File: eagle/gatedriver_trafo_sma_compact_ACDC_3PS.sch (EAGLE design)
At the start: 25 parts, among them IC1 ISO1540, T1 TIP122V, T3 TIP122V, X1 BU-SMA-V

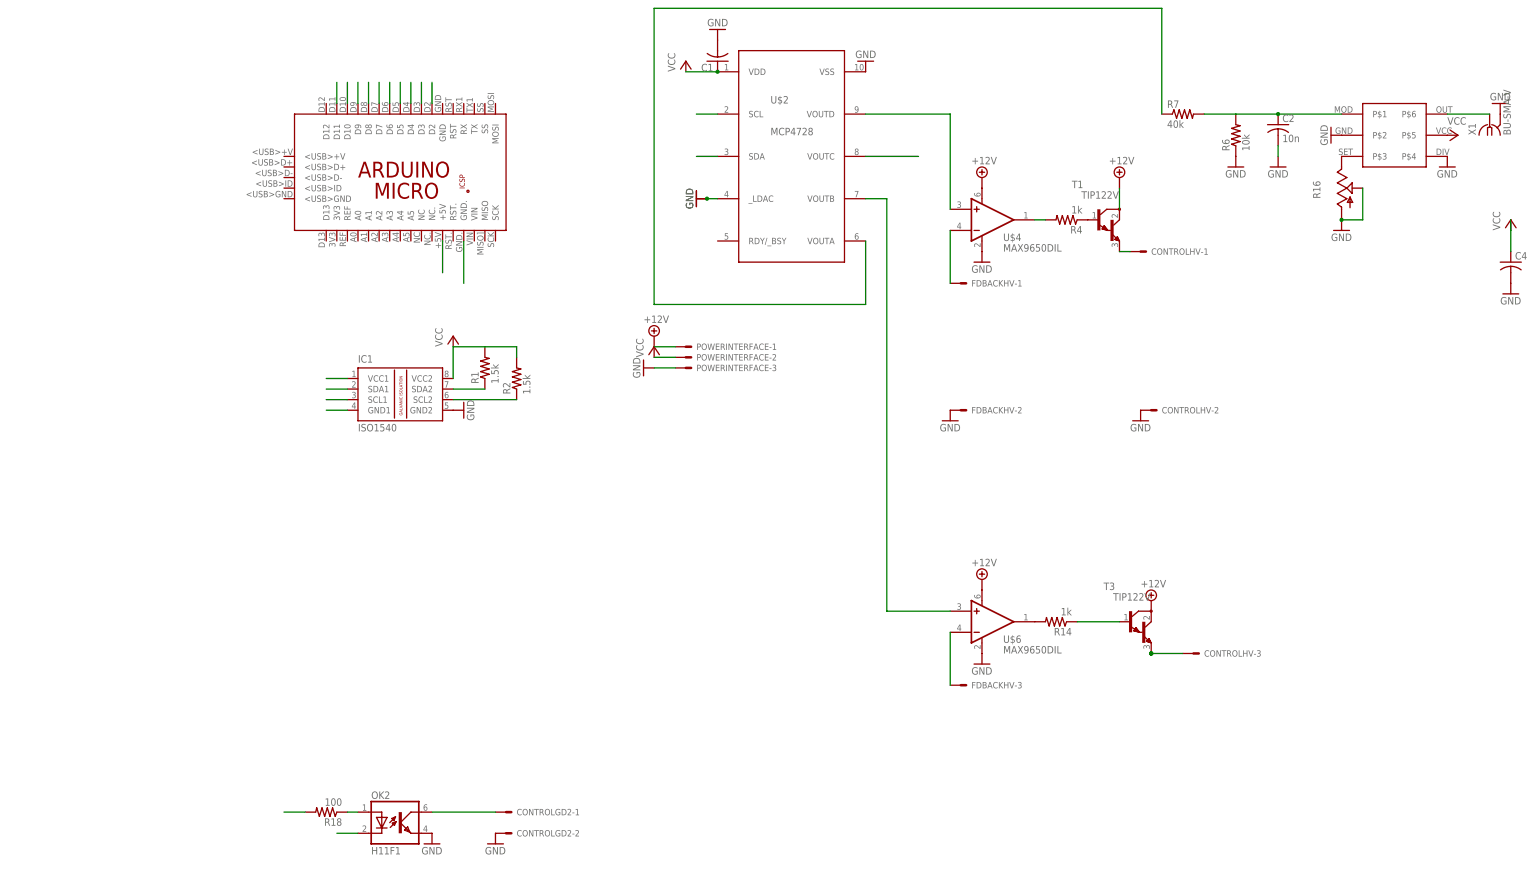
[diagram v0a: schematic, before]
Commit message: 3PS, 2 1kV in parallel
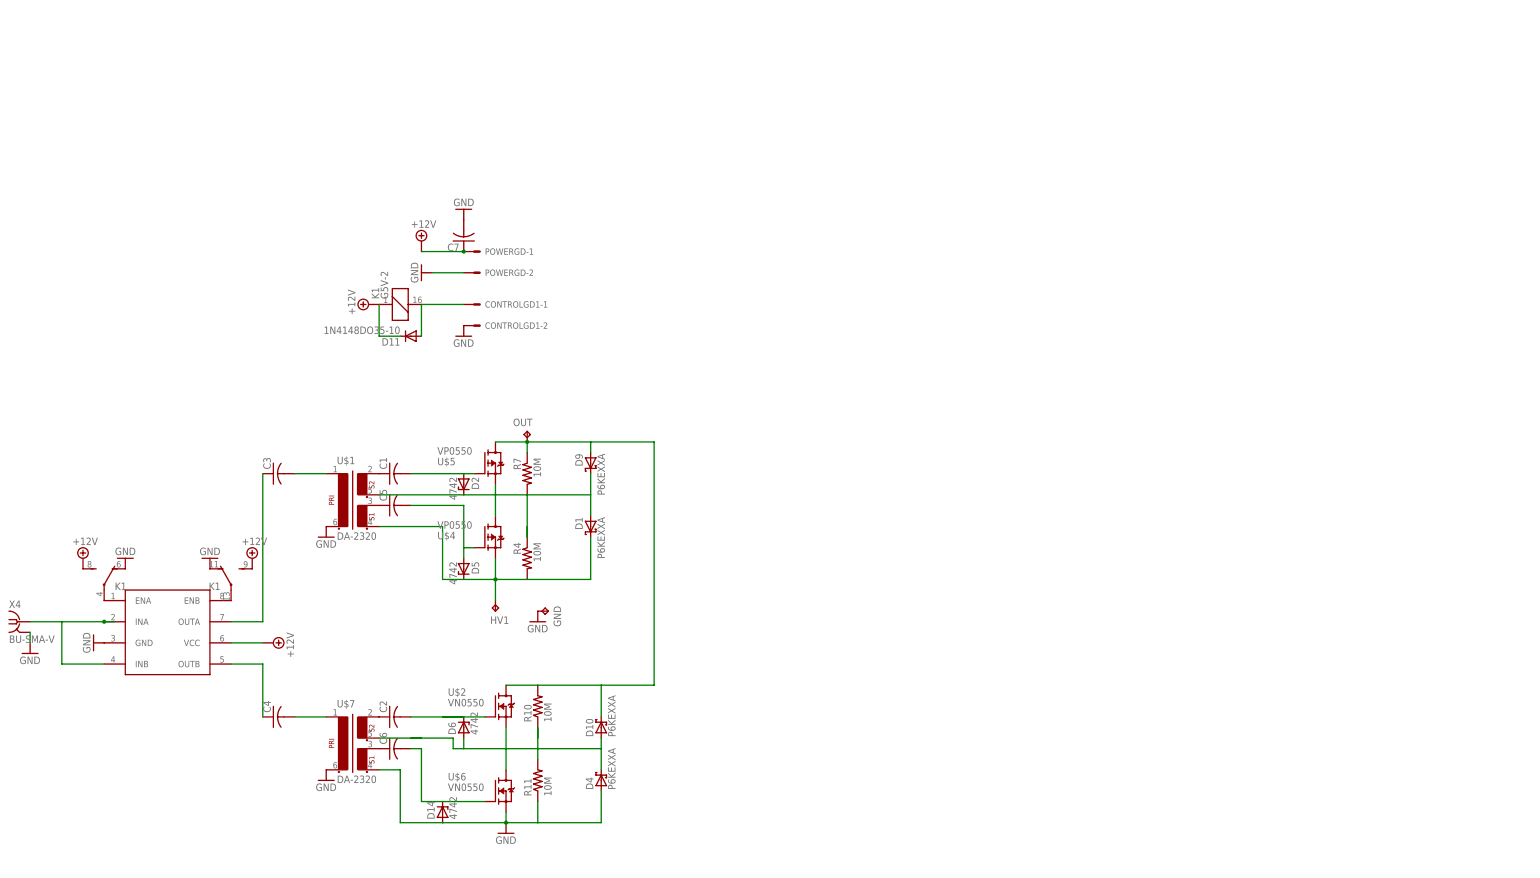
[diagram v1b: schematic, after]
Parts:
- removed CONTROLGD2: (no value), con-molex:KK-156-2
- removed CONTROLHV, FDBACKHV, POWERINTERFACE: (no value), con-molex:KK-156-3
- removed IC1: ISO1540, texas:ISO1540
- removed OK2: H11F1, optocoupler:H11F1
- removed PCB1: ARDUINO_MICRO, E14_Arduino_published:ARDUINO_MICRO
- removed R1, R2: 1.5k, resistor:R-US_0207/12
- removed R14: 1k, resistor:R-US_0207/12
- removed R16: (no value), pot:TRIM_US-B90P
- removed R18: 100, rcl:R-US_0207/12
- removed R6: 10k, resistor:R-US_0207/12
- removed T1, T3: TIP122V, transistor-npn:TIP122V
- removed X1: BU-SMA-V, con-coax:BU-SMA-V
- added C3, C5, C6: (no value), resistor:C-US050-055X075
- added C7: (no value), rcl:C-US050-030X075
- added CONTROLGD1, POWERGD: (no value), con-molex:KK-156-2
- added D1, D10, D4, D9: P6KEXXA, diode:P6KEXXA
- added D11: 1N4148DO35-10, diode:1N4148DO35-10
- added D14, D2, D5, D6: 4742, diode:ZENER-DIODEZD-10
- added GND, HV1, OUT: TPPAD1-20Y, testpad:TPPAD1-20Y
- added K1: G5V-2, relay:G5V-2
- added R10, R11: 10M, rcl:R-US_0207/12
- added U$3: UCC27425, texas:UCC27425
- added U$5: VP0550, transistor-fet:VP0550
- added U$7: DA-2320, trafo:DA-2320
- added X4: BU-SMA-V, con-coax:BU-SMA-V
- C1: device rcl:C-US050-050X075 -> resistor:C-US050-055X075
- C2: value 10n -> (none); device resistor:C-US050-024X044 -> resistor:C-US050-055X075
- C4: device resistor:C-US075-063X106 -> resistor:C-US050-055X075
- R4: value 1k -> 10M; device resistor:R-US_0207/12 -> rcl:R-US_0207/12
- R7: value 40k -> 10M; device resistor:R-US_0207/12 -> rcl:R-US_0207/12
- U$1: value LTC6992 -> DA-2320; device linear-technology:LTC6992 -> trafo:DA-2320
- U$2: value MCP4728DIL -> VN0550; device microchip:MCP4728DIL -> transistor-fet:VN0550
- U$4: value MAX9650DIL -> VP0550; device maxim:MAX9650DIL -> transistor-fet:VP0550
- U$6: value MAX9650DIL -> VN0550; device maxim:MAX9650DIL -> transistor-fet:VN0550
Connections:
- removed net +12V: POWERINTERFACE-1.S, T1.C, T3.C, U$4.V+, U$6.V+
- removed net A+5: IC1.VCC1, PCB1.+5V
- removed net AGND: IC1.GND1, PCB1.GND., R18.2
- removed net D10: PCB1.D10
- removed net D11: PCB1.D11
- removed net D4: PCB1.D4
- removed net D7: PCB1.D7
- removed net D8: PCB1.D8
- removed net ENSW2: CONTROLGD2-1.S, OK2.COL
- removed net N$12: R16.E, U$1.P$3
- removed net N$19: R4.2, U$4.OUT
- removed net N$8: FDBACKHV-1.S, U$4.-IN
- removed net PWM5: PCB1.D5
- removed net PWM6: PCB1.D6
- removed net PWM9: OK2.C, PCB1.D9
- removed net SCL: IC1.SCL1, PCB1.D3
- removed net SCL_OUT: IC1.SCL2, R2.1, U$2.SCL
- removed net SDA: IC1.SDA1, PCB1.D2
- removed net SDA_OUT: IC1.SDA2, R1.1, U$2.SDA
- removed net VCC: C1.1, C4.1, IC1.VCC2, POWERINTERFACE-2.S, R1.2, R2.2, U$1.P$5, U$2.VDD
- new net +15V: C7.1, D11.C, K11.S, K12.S, K1A.1, POWERGD-1.S, U$3.VCC
- new net ENSW: CONTROLGD1-1.S, D11.A, K1A.2
- new net N$11: C1.2, D2.A, U$5.G
- new net N$22: C2.1, U$7.6
- new net N$23: C6.1, U$7.4
- new net N$25: C2.2, D6.C, U$2.G
- new net N$27: C6.2, D14.C, U$6.G
- new net N$6: C4.2, U$7.1
- new net N$9: U$7.5
- net GND: now also C7.2, CONTROLGD1-2.S, D14.A, D4.A, GND.TP, K11.O, K12.O, POWERGD-2.S, R11.1, U$1.2, U$3.GND, U$6.S, U$7.2, U$7.3, X4.2; no longer C1.2, C2.2, C4.2, CONTROLGD2-2.S, CONTROLHV-2.S, FDBACKHV-2.S, IC1.GND2, OK2.EMIT, POWERINTERFACE-3.S, R16.A, R16.S, R6.1, U$1.P$2, U$1.P$4, U$2.VSS, U$2._LDAC, U$4.V-, U$6.V-, X1.2
- net N$1: now also U$3.INA, U$3.INB, X4.1; no longer R7.1, U$2.VOUTA
- net N$13: now also D10.A, D4.C, D6.A, R10.1, R11.2, U$2.S, U$6.D; no longer U$1.P$6, X1.1
- net N$14: now also K11.P, U$3.ENA; no longer FDBACKHV-3.S, U$6.-IN
- net N$15: now also K12.P, U$3.ENB; no longer R14.1, T3.B
- net N$16: now also C5.2, D5.A, U$4.G; no longer U$2.VOUTD, U$4.+IN
- net N$17: now also D1.C, D5.C, HV1.TP, R4.2, U$1.3, U$4.S; no longer U$2.VOUTC
- net N$18: now also D1.A, D2.C, D9.C, R4.1, R7.2, U$1.5, U$4.D, U$5.S; no longer U$2.VOUTB, U$6.+IN
- net N$2: now also C3.1, U$3.OUTA; no longer C2.1, R6.2, R7.2, U$1.P$1
- net N$21: now also D10.C, D9.A, OUT.TP, R10.2, R7.1, U$2.D, U$5.D; no longer R14.2, U$6.OUT
- net N$3: now also C3.2, U$1.1; no longer R4.1, T1.B
- net N$4: now also C4.1, U$3.OUTB; no longer CONTROLHV-1.S, T1.E
- net N$5: now also C1.1, U$1.6; no longer CONTROLHV-3.S, T3.E
- net N$7: now also C5.1, U$1.4; no longer OK2.A, R18.1
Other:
- moved on the sheet: C1, C2, C4, R4, R7

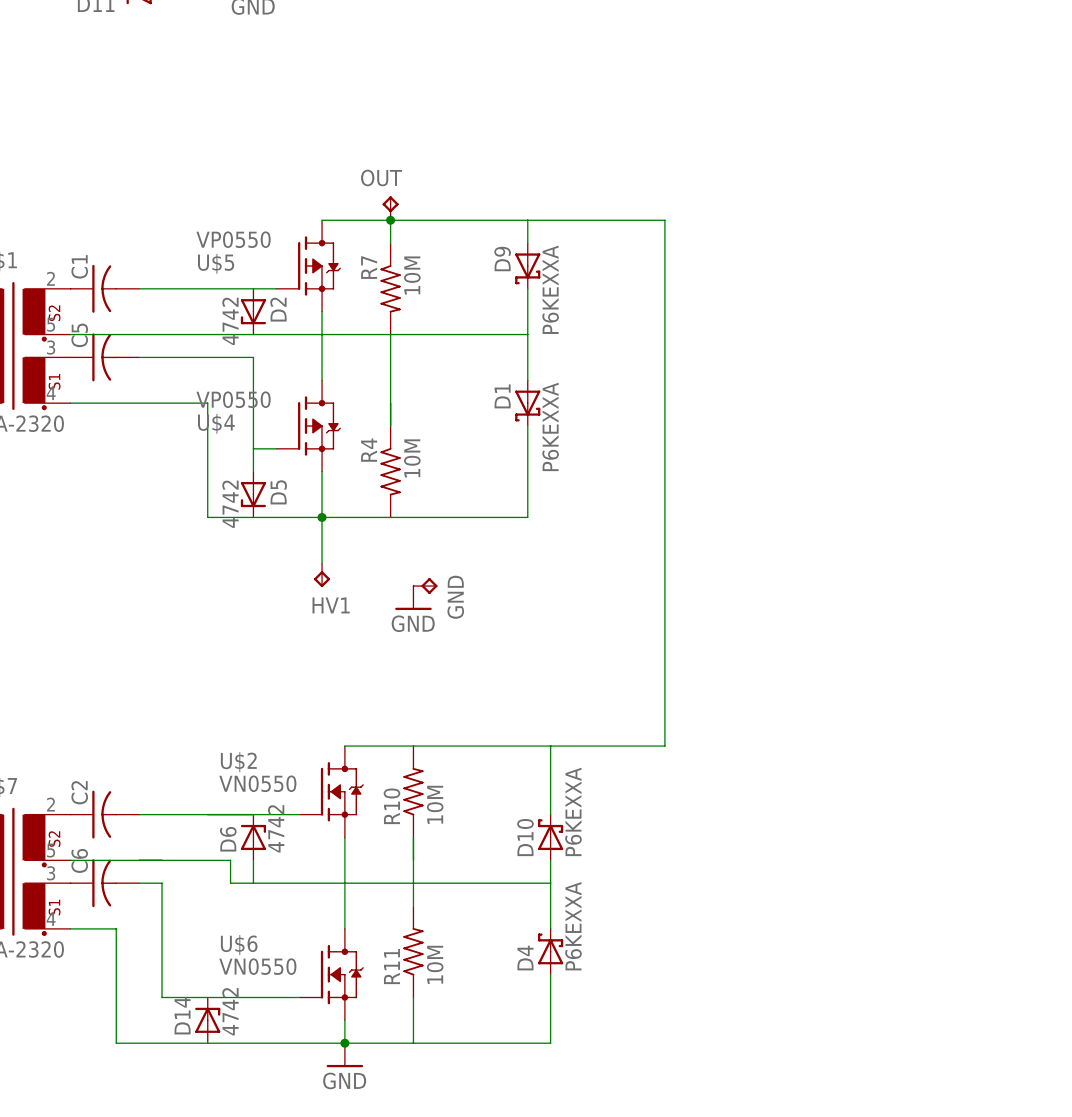
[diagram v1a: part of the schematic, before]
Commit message: capacitor bank
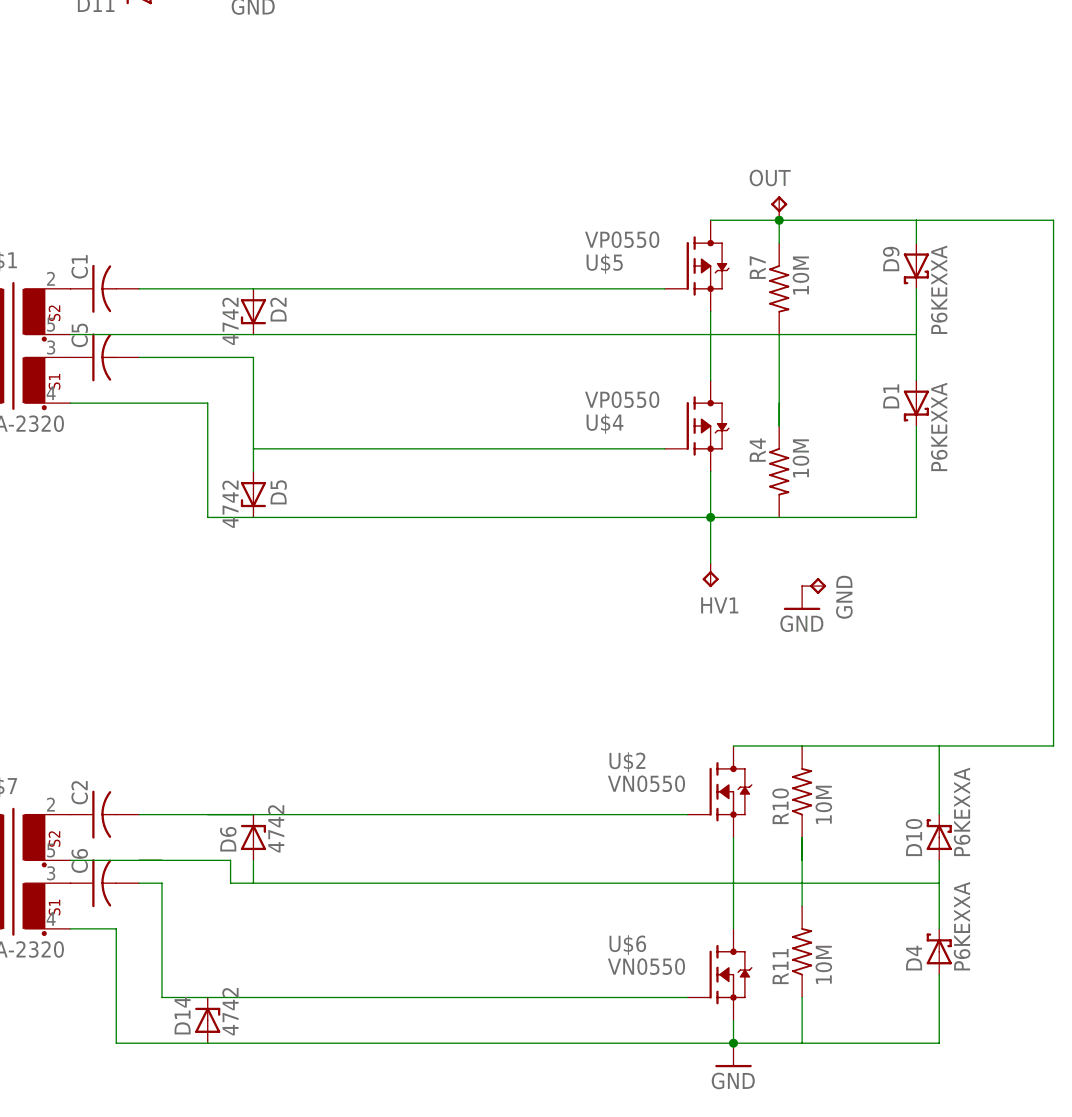
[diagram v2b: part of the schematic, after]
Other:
- moved on the sheet: D1, D10, D4, D9, GND, HV1, OUT, R10, R11, R4, R7, U$2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

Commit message: IXYS board solution, gatedriver components
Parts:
- added C8: (no value), resistor:C-US102-064X133
- added R1, R12, R2, R3, R5, R6, R8, R9: 1M, rcl:R-US_0207/10
- added R13, R14: 1M, rcl:R-US_0207/12
- R10, R11, R4, R7: value 10M -> 1M; device rcl:R-US_0207/12 -> rcl:R-US_0207/10
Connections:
- new net N$10: C1.2, D2.A, R6.1
- new net N$12: R2.1, R8.2, U$4.G
- new net N$19: C3.2, R13.2
- new net N$20: C4.2, R14.2
- new net N$8: R1.1, R6.2, U$5.G
- net GND: now also C8.2
- net N$11: now also R12.2, R5.1, U$6.G; no longer C1.2, D2.A, U$5.G
- net N$16: now also R8.1; no longer U$4.G
- net N$17: now also C8.1, R2.2
- net N$18: now also R1.2
- net N$25: now also R3.1, R9.1, R9.2
- net N$27: now also R12.1; no longer U$6.G
- net N$3: now also R13.1; no longer C3.2
- net N$6: now also R14.1; no longer C4.2
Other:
- moved on the sheet: C1, C2, C3, C4, C5, C6, D14, D2, D5, D6, GND, HV1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
